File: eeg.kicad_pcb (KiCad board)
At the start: 6 copper layers, 35 x 23 mm, 71 parts, among them IC1 NPM1300, IC2 LM2664M6X_NOPB, IC3 ADS1299-4PAGR, J1 Conn_01x03, J2 Conn_01x04, J3 USB-C Connectors, J4 Conn_01x06, SW1 SW_SPDT, U1 NRF5340, U2 BMI270

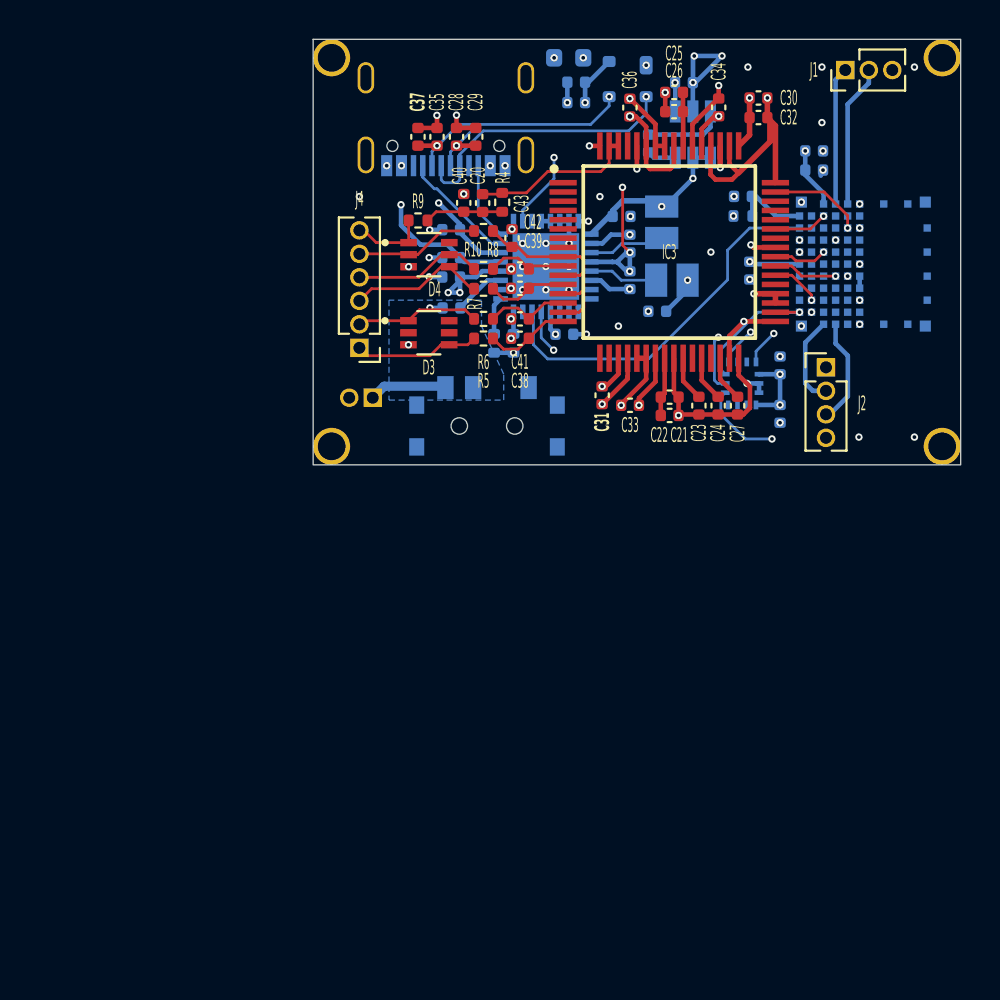
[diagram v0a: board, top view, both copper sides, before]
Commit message: Feat: 개발보드 버전으로 PCB 변경
수정사항

단가 감소
- PCB Board size up (50x50)
- blind via 제거 (전체 레이아웃 수정)
- AVDD 전력평면 추가
- ADS1299 안쓰는핀 GND
- ADS1299 배치 변경 (Layout Reference 적용)

개발보드만 적용사항
- Pin Header size up 1.27 → 2.54mm
- PCB Size 50x50(mm)
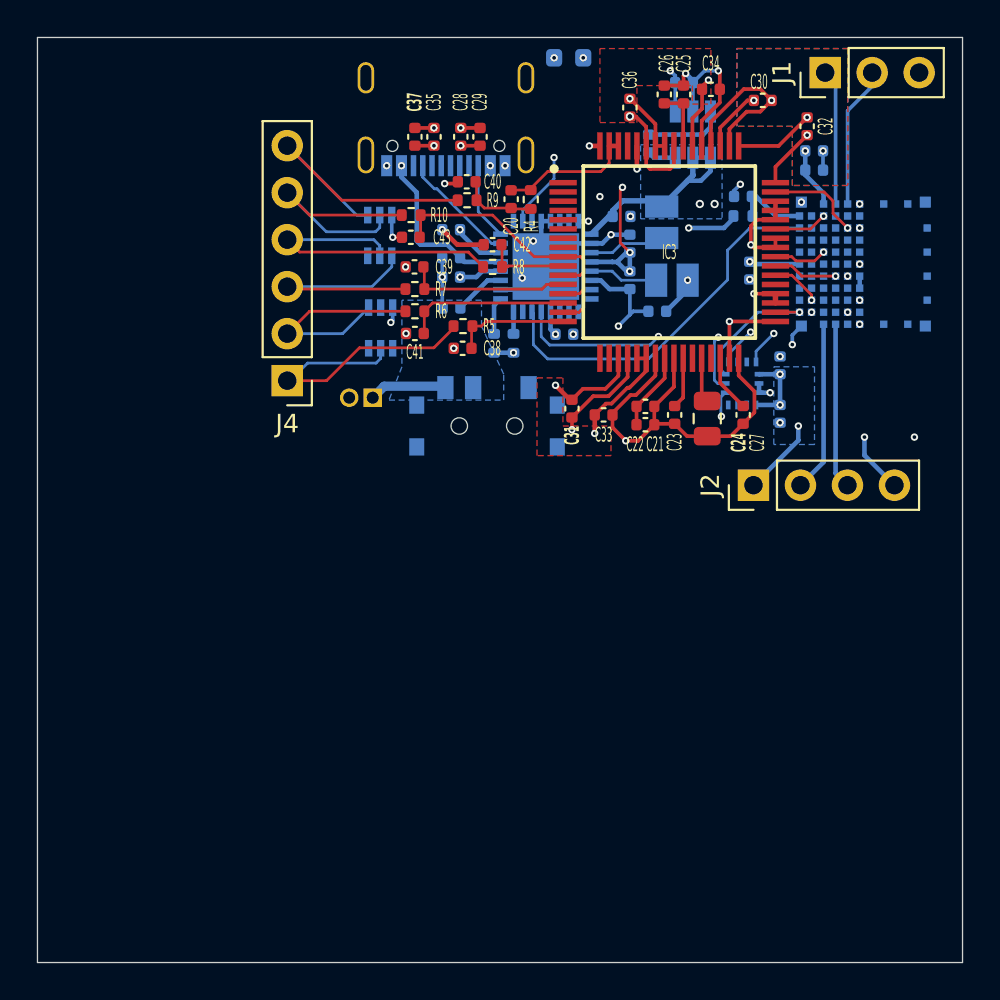
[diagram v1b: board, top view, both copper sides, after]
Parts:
- removed C14: 1uF, Capacitor_SMD:C_0402_1005Metric
- removed C16: 100nF, Capacitor_SMD:C_0402_1005Metric
- removed D4: TPD4E1B06DCKR, TPD4E1B06DCKR:TVS_TPD4E1B06DCKR
- removed EEG_Board1: PCB Edge, MountingHole:eeg
- C24: footprint Capacitor_SMD:C_0402_1005Metric -> Capacitor_SMD:C_0805_2012Metric
- D2: value PRTR5V0U2X -> TPD4E1B06DCKR; footprint Package_TO_SOT_SMD:SOT-143 -> TPD4E1B06DCKR:TVS_TPD4E1B06DCKR
- D3: moved to B.Cu
- J1: footprint Connector_PinHeader_1.27mm:PinHeader_1x03_P1.27mm_Vertical -> Connector_PinHeader_2.54mm:PinHeader_1x03_P2.54mm_Vertical
- J2: footprint Connector_PinHeader_1.27mm:PinHeader_1x04_P1.27mm_Vertical -> Connector_PinHeader_2.54mm:PinHeader_1x04_P2.54mm_Vertical
- J4: footprint Connector_PinHeader_1.27mm:PinHeader_1x06_P1.27mm_Vertical -> Connector_PinHeader_2.54mm:PinHeader_1x06_P2.54mm_Vertical
- moved D2 19.0 mm to (136.2, 104.1), turned to -90 degrees
- moved J2 7.48 mm to (156.3, 112.6), turned to 90 degrees
- moved D3 5.89 mm to (136.1, 99.1), turned to -90 degrees
- moved C39 5.82 mm to (138.0, 100.8)
- moved C41 5.73 mm to (138.0, 104.4)
- moved C43 5.47 mm to (137.8, 99.2), turned to 0 degrees
- moved J4 4.28 mm to (131.1, 107.0)
- moved R10 4.00 mm to (137.8, 98.0)
- moved R6 3.73 mm to (138.0, 103.2)
- moved R7 3.71 mm to (138.0, 102.0)
- moved C38 3.15 mm to (140.6, 105.2)
- moved R9 2.87 mm to (140.8, 97.2)
- moved C32 2.67 mm to (159.2, 93.2), turned to -90 degrees
- moved C42 1.98 mm to (142.2, 99.6)
- moved C31 1.78 mm to (146.5, 108.5)
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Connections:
- D2 pad 1: GND -> /ads1299/2P
- D2 pad 2: /USB-C/DP1 -> unconnected-(D2-Pad2)
- D2 pad 3: /USB-C/DN1 -> GND
- D2 pad 4: /USB-C/VBUS_IN -> unconnected-(D2-Pad4)
- D3 pad 1: /ads1299/2P -> /ads1299/BIAS
- D3 pad 2: unconnected-(D3-Pad2) -> /ads1299/REF
- D3 pad 4: /ads1299/1P -> /ads1299/3P
- D3 pad 5: unconnected-(D3-Pad5) -> /ads1299/4P
- IC3 pad 42: unconnected-(IC3-GPIO1-Pad42) -> GND
- IC3 pad 44: unconnected-(IC3-GPIO2-Pad44) -> GND
- IC3 pad 45: unconnected-(IC3-GPIO3-Pad45) -> GND
- IC3 pad 46: unconnected-(IC3-GPIO4-Pad46) -> GND
- J3 pad A6: /USB-C/DP1 -> unconnected-(J3-DP1-PadA6)
- J3 pad A7: /USB-C/DN1 -> unconnected-(J3-DN1-PadA7)
- J3 pad B6: /USB-C/DP1 -> unconnected-(J3-DP2-PadB6)
- J3 pad B7: /USB-C/DN1 -> unconnected-(J3-DN2-PadB7)
- U1 pad A4: /USB-C/DP1 -> unconnected-(U1-D+-PadA4)
- U1 pad A5: /USB-C/DN1 -> unconnected-(U1-D--PadA5)
- U1 pad D4: /nrf5340/BMI270_CS -> unconnected-(U1-P0.18/QSPI_CS-PadD4)
- U1 pad E10: unconnected-(U1-P0.26/AIN5-PadE10) -> /nrf5340/BMI270_CS
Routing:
- net /USB-C/DN1: track 29.8 -> 0.00 mm, vias 2 -> 0
- net /USB-C/DP1: track 27.8 -> 0.00 mm, vias 2 -> 0
- net GND: track 30.2 -> 57.0 mm, vias 64 -> 42
- net /ads1299/BIAS: track 4.14 -> 16.3 mm
- net /nrf5340/BMI270_CS: track 21.1 -> 10.6 mm
- net VSSA: track 31.3 -> 41.8 mm, vias 10 -> 6
- net /USB-C/VBUS_IN: track 19.3 -> 9.42 mm, vias 4 -> 2
- net /ads1299/4P: track 7.17 -> 16.9 mm
- net /ads1299/1P: track 6.76 -> 16.4 mm
- net /ads1299/REF: track 6.75 -> 13.3 mm
- net /ads1299/3P: track 7.46 -> 13.1 mm
- net /ads1299/E_REFERENCE: track 11.8 -> 17.2 mm
- net /ads1299/2P: track 6.73 -> 11.9 mm
- net /ads1299/IN3P: track 4.36 -> 8.83 mm
- net /SWDIO: track 4.89 -> 9.22 mm
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- added copper zone on B.Cu, net /AVDD
- added copper zone on F.Cu, net /AVDD
- added copper zone on B.Cu, net /DVDD
- added copper zone on F.Cu, net /DVDD
- added copper zone on In3.Cu, net /DVDD
- removed copper zone on In3.Cu, net VSSA
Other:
- board size 35 x 23 mm -> 50 x 50 mm

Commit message: Doc: Gerber Data V0.2(dev)
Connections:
- IC3 pad 42: GND -> unconnected-(IC3-GPIO1-Pad42)
- IC3 pad 44: GND -> unconnected-(IC3-GPIO2-Pad44)
- IC3 pad 45: GND -> unconnected-(IC3-GPIO3-Pad45)
- IC3 pad 46: GND -> unconnected-(IC3-GPIO4-Pad46)
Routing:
- net GND: track 57.0 -> 53.0 mm
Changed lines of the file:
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@@
 	(net 141 "unconnected-(U1-P0.30-PadE2)")
 	(net 142 "unconnected-(U1-P1.06-PadF2)")
+	(net 143 "unconnected-(IC3-GPIO4-Pad46)")
+	(net 144 "unconnected-(IC3-GPIO1-Pad42)")
+	(net 145 "unconnected-(IC3-GPIO3-Pad45)")
+	(net 146 "unconnected-(IC3-GPIO2-Pad44)")
 	(footprint "Connector_PinHeader_2.54mm:PinHeader_1x04_P2.54mm_Vertical"
 		(locked yes)
@@
 			(size 0.3 1.475)
 			(layers "F.Cu" "F.Paste" "F.Mask")
-			(net 36 "GND")
+			(net 144 "unconnected-(IC3-GPIO1-Pad42)")
 			(pinfunction "GPIO1")
-			(pintype "passive")
+			(pintype "passive+no_connect")
 		)
 		(pad "43" smd rect
@@
 			(size 0.3 1.475)
 			(layers "F.Cu" "F.Paste" "F.Mask")
-			(net 36 "GND")
+			(net 146 "unconnected-(IC3-GPIO2-Pad44)")
 			(pinfunction "GPIO2")
-			(pintype "passive")
+			(pintype "passive+no_connect")
 		)
 		(pad "45" smd rect
@@
 			(size 0.3 1.475)
 			(layers "F.Cu" "F.Paste" "F.Mask")
-			(net 36 "GND")
+			(net 145 "unconnected-(IC3-GPIO3-Pad45)")
 			(pinfunction "GPIO3")
-			(pintype "passive")
+			(pintype "passive+no_connect")
 		)
 		(pad "46" smd rect
@@
 			(size 0.3 1.475)
 			(layers "F.Cu" "F.Paste" "F.Mask")
-			(net 36 "GND")
+			(net 143 "unconnected-(IC3-GPIO4-Pad46)")
 			(pinfunction "GPIO4")
-			(pintype "passive")
+			(pintype "passive+no_connect")
 		)
 		(pad "47" smd rect
@@
 	)
 	(segment
-		(start 157.488 98.25)
-		(end 156.5005 98.25)
-		(width 0.2)
-		(locked yes)
-		(layer "F.Cu")
-		(net 36)
-	)
-	(segment
 		(start 154.5 94.262)
 		(end 154.5 93.2745)
@@
 	)
 	(segment
-		(start 157.488 97.25)
-		(end 157.488 98.25)
-		(width 0.25)
-		(locked yes)
-		(layer "F.Cu")
-		(net 36)
-	)
-	(segment
 		(start 148 94.262)
 		(end 147.432 94.262)
@@
 	)
 	(segment
-		(start 156.5005 98.25)
-		(end 156.16 98.5905)
-		(width 0.2)
-		(locked yes)
-		(layer "F.Cu")
-		(net 36)
-	)
-	(segment
-		(start 157.488 99.25)
-		(end 157.488 99.75)
-		(width 0.2)
-		(locked yes)
-		(layer "F.Cu")
-		(net 36)
-	)
-	(segment
 		(start 155.5 94.262)
 		(end 157.658 94.262)
@@
 		(locked yes)
 		(layer "F.Cu")
-		(net 36)
-	)
-	(segment
-		(start 156.16 98.5905)
-		(end 156.16 99.61)
-		(width 0.2)
-		(locked yes)
-		(layer "F.Cu")
